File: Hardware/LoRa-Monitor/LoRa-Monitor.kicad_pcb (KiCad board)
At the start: 2 copper layers, 1.4 x 13 mm, 222 parts, among them J1 USB_C_Receptacle_USB2.0_16P, J10 AudioJack3, J11 Screw_Terminal_01x02, J12 Screw_Terminal_01x02, J13 Conn_01x02_Pin, J14 Conn_01x02_Pin, J2 Micro_SD_Card, J3 Conn_02x03_Odd_Even, J4 Conn_Coaxial, J5 Screw_Terminal_01x02, J6 Screw_Terminal_01x02, J7 AudioJack3, J8 AudioJack3, J9 Screw_Terminal_01x04, Q1 ZXTN25100DFH, Q2 ZXTN25100DFH, Q3 ZXTN25100DFH, Q4 ZXTN25100DFH, Q5 ZXTN25100DFH, Q6 ZXTN25100DFH, U1 IRM-05-5, U10 ESP32-S3-WROOM-1, U11 TPS63021DSJR, U12 NXE1S0303MC, U13 NXE1S0303MC, U14 ATM90E32AS-AU-R, U15 E22-900M30S, U16 ADuM1401xRW, U17 ADuM1401xRW, U18 ADuM1401xRW, U2 ACPL-M61L, U3 ACPL-M61L, U4 ACPL-M61L, U5 ACPL-M61L, U6 ACPL-M61L, U7 ACPL-M61L, U8 MAX3483, U9 BQ24072RGT

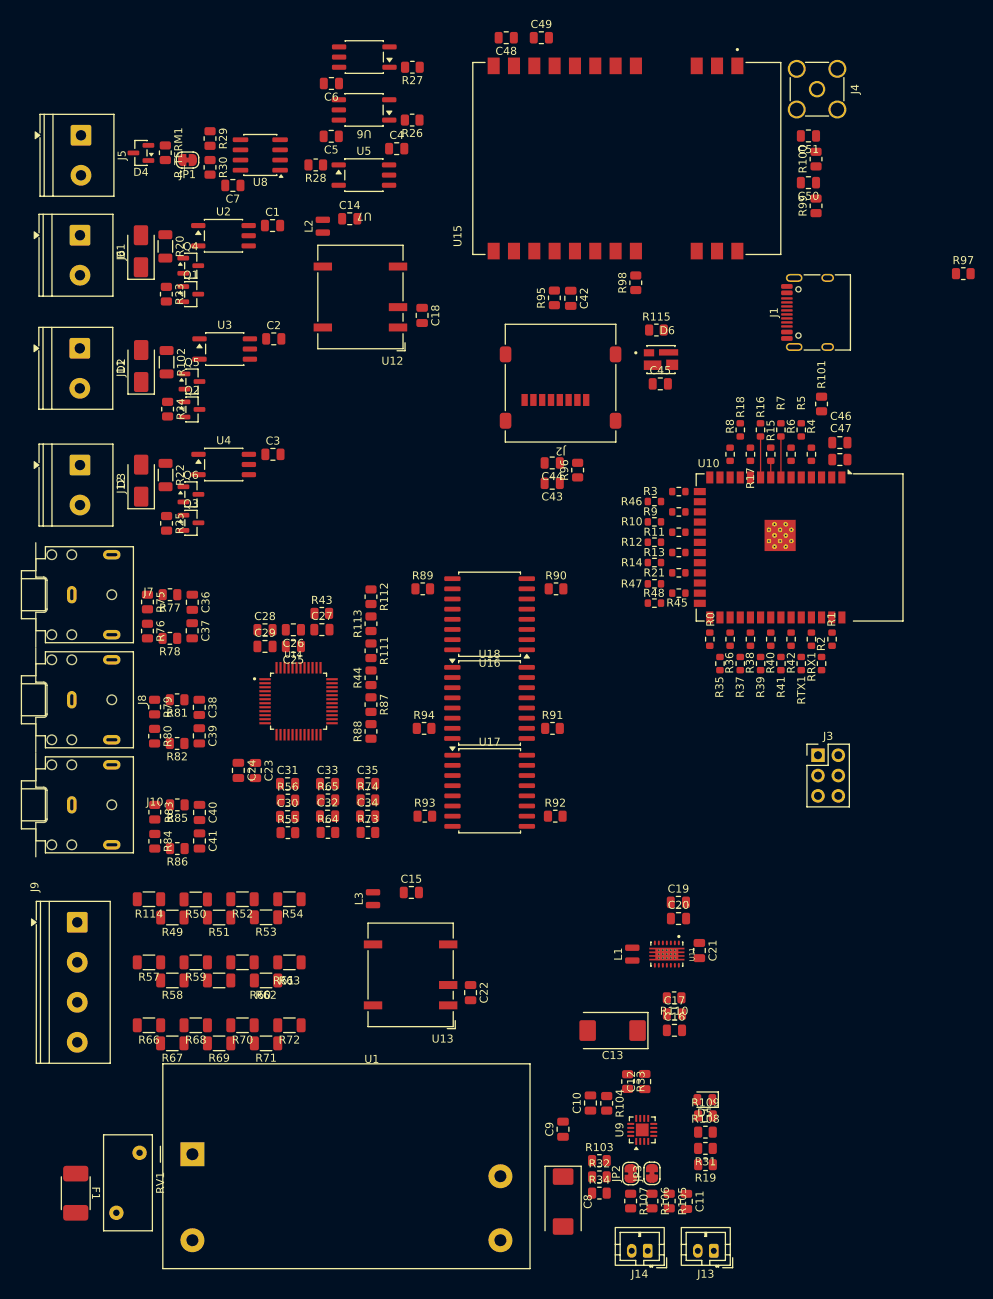
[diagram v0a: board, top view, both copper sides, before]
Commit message: Fixed schematics and started layout
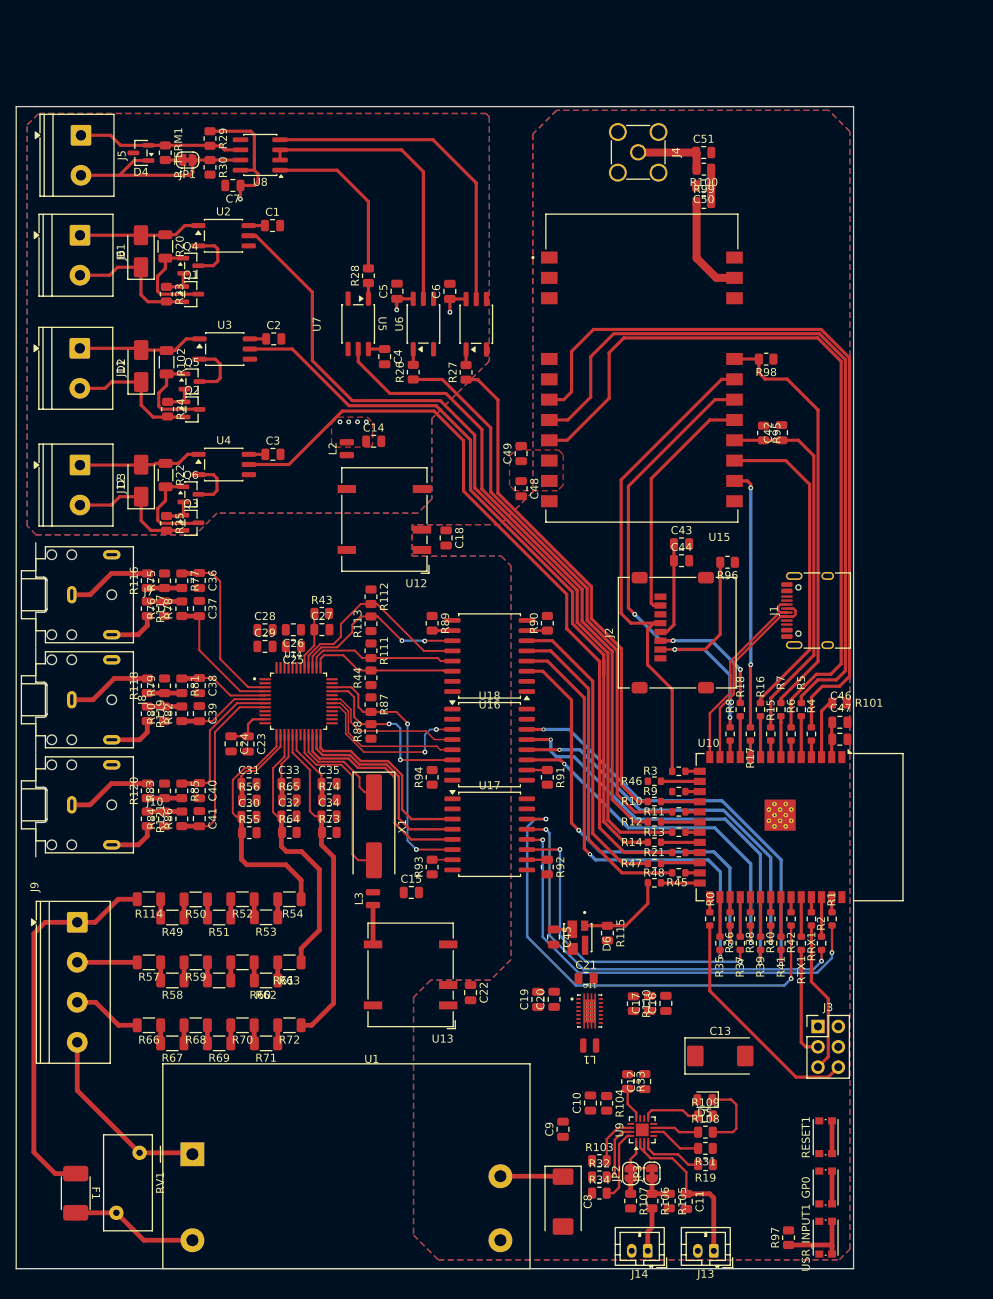
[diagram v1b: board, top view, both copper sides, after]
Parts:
- added GP0: SW_Push, Button_Switch_SMD:SW_Push_1P1T_NO_CK_KMR2, F.Cu at (130.2, 159.9)
- added R116: 0R, Resistor_SMD:R_0805_2012Metric, F.Cu at (45.4, 84.1)
- added R117: 0R, Resistor_SMD:R_0805_2012Metric, F.Cu at (45.4, 87.6)
- added R118: 0R, Resistor_SMD:R_0805_2012Metric, F.Cu at (45.4, 97.2)
- added R119: 0R, Resistor_SMD:R_0805_2012Metric, F.Cu at (45.4, 100.7)
- added R120: 0R, Resistor_SMD:R_0805_2012Metric, F.Cu at (45.4, 110.4)
- added R121: 0R, Resistor_SMD:R_0805_2012Metric, F.Cu at (45.4, 113.9)
- added RESET1: SW_Push, Button_Switch_SMD:SW_Push_1P1T_NO_CK_KMR2, F.Cu at (130.2, 153.7)
- added USR_INPUT1: SW_Push, Button_Switch_SMD:SW_Push_1P1T_NO_CK_KMR2, F.Cu at (130.2, 166.2)
- added X1: 16.384MHz, Crystal:Crystal_SMD_HC49-SD, F.Cu at (73.7, 114.8)
- moved R97 122.5 mm to (125.5, 166.2), turned to 90 degrees
- moved R115 75.6 mm to (102.9, 128.2), turned to -90 degrees
- moved D6 73.0 mm to (99.2, 128.7), turned to -90 degrees
- moved C45 70.4 mm to (96.2, 128.6), turned to -90 degrees
- moved C48 56.4 mm to (92.1, 72.6), turned to -90 degrees
- moved C49 52.0 mm to (92.1, 68.2), turned to 90 degrees
- moved R27 38.7 mm to (85.2, 58.1), turned to 90 degrees
- moved R101 37.5 mm to (131.9, 99.4), turned to 0 degrees
- moved J1 37.3 mm to (129.4, 87.8)
- moved U7 36.2 mm to (86.5, 52.0), turned to 90 degrees
- moved C46 35.0 mm to (131.9, 101.8)
- moved C47 35.0 mm to (131.9, 103.9)
- moved R0 35.0 mm to (115.7, 126.4)
- moved R1 35.0 mm to (131.0, 126.4)
- moved R10 35.0 mm to (108.8, 111.7)
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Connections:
- net Net-(R46-Pad2) renamed /MCU/USR_IN
- R18 pad 2: /MCU/CS_SD -> /MCU/SDO_SPI1
- R75 pad 1: /Connectors/IA+ -> Net-(R116-Pad1)
- R76 pad 2: /Connectors/IA- -> Net-(R117-Pad1)
- R77 pad 2: /Connectors/IA+ -> Net-(R116-Pad1)
- R78 pad 2: /Connectors/IA- -> Net-(R117-Pad1)
- R79 pad 1: /Connectors/IB+ -> Net-(R118-Pad1)
- R8 pad 1: /MCU/SDO_SPI1 -> /MCU/CS_SD
- R80 pad 2: /Connectors/IB- -> Net-(R119-Pad1)
- R81 pad 2: /Connectors/IB+ -> Net-(R118-Pad1)
- R82 pad 2: /Connectors/IB- -> Net-(R119-Pad1)
- R83 pad 1: /Connectors/IC+ -> Net-(R120-Pad1)
- R84 pad 2: /Connectors/IC- -> Net-(R121-Pad1)
- R85 pad 2: /Connectors/IC+ -> Net-(R120-Pad1)
- R86 pad 2: /Connectors/IC- -> Net-(R121-Pad1)
- U17 pad 11: /Energy meter/ZX0 -> /Energy meter/PM1
- U17 pad 12: /Energy meter/ZX1 -> /Energy meter/ZX0
- U17 pad 13: /Energy meter/ZX2 -> /Energy meter/ZX1
- U17 pad 14: /Energy meter/WARNOUT -> /Energy meter/ZX2
- U17 pad 3: /Energy meter/WARNOUT_M90 -> /Energy meter/ZX2_M90
- U17 pad 4: /Energy meter/ZX2_M90 -> /Energy meter/ZX1_M90
- U17 pad 5: /Energy meter/ZX1_M90 -> /Energy meter/ZX0_M90
- U17 pad 6: /Energy meter/ZX0_M90 -> /Energy meter/PM1_M90
- U18 pad 11: /Energy meter/IRQ0 -> /Energy meter/PM0
- U18 pad 12: /Energy meter/IRQ1 -> /Energy meter/IRQ0
- U18 pad 13: /Energy meter/PM0 -> /Energy meter/IRQ1
- U18 pad 14: /Energy meter/PM1 -> /Energy meter/WARNOUT
- U18 pad 3: /Energy meter/PM1_M90 -> /Energy meter/WARNOUT_M90
- U18 pad 4: /Energy meter/PM0_M90 -> /Energy meter/IRQ1_M90
- U18 pad 5: /Energy meter/IRQ1_M90 -> /Energy meter/IRQ0_M90
- U18 pad 6: /Energy meter/IRQ0_M90 -> /Energy meter/PM0_M90
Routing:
- net /Energy Meter Interface Module/PULSE_IN1_3V3: track 0.00 -> 107.3 mm
- net /Energy Meter Interface Module/PULSE_IN3_3V3: track 0.00 -> 96.9 mm
- net /LoRa Module/DIO2_E22: track 0.00 -> 95.7 mm
- net /Energy Meter Interface Module/PULSE_IN2_3V3: track 0.00 -> 95.4 mm
- net /LoRa Module/RXEN_E22: track 0.00 -> 95.0 mm
- net /LoRa Module/TXEN_E22: track 0.00 -> 92.3 mm
- net /Energy Meter Interface Module/RXD_485: track 0.00 -> 79.2 mm
- net /Energy Meter Interface Module/EN_485: track 0.00 -> 72.3 mm
- net /Energy Meter Interface Module/TXD_485: track 0.00 -> 63.7 mm
- net /MCU/SCLK_SPI1: track 0.00 -> 62.4 mm
- net /Energy meter/ZX2: track 0.00 -> 61.4 mm, vias 0 -> 2
- net /Energy meter/SCKL_SPI0: track 0.00 -> 57.6 mm, vias 0 -> 2
- net /Energy meter/ZX0: track 0.00 -> 57.0 mm, vias 0 -> 2
- net /Energy meter/CS_ATM90: track 0.00 -> 56.6 mm, vias 0 -> 2
- net /MCU/SDO_SPI1: track 0.00 -> 55.9 mm, vias 0 -> 3
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- added copper zone on F.Cu, net +3.3V
- added copper zone on F.Cu, net +3.3V_485
- added copper zone on In2.Cu, net +3.3V_485
- added copper zone on B.Cu, net GND
- added copper zone on F.Cu, net GND
- added copper zone on In1.Cu, net GND
- added copper zone on B.Cu, net GND_485
- added copper zone on F.Cu, net GND_485
- added copper zone on In1.Cu, net GND_485
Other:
- board size 1.4 x 13 mm -> 104.7 x 145.3 mm
- copper layers 2 -> 4

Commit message: Finished routing and DRC gives 0 errors.
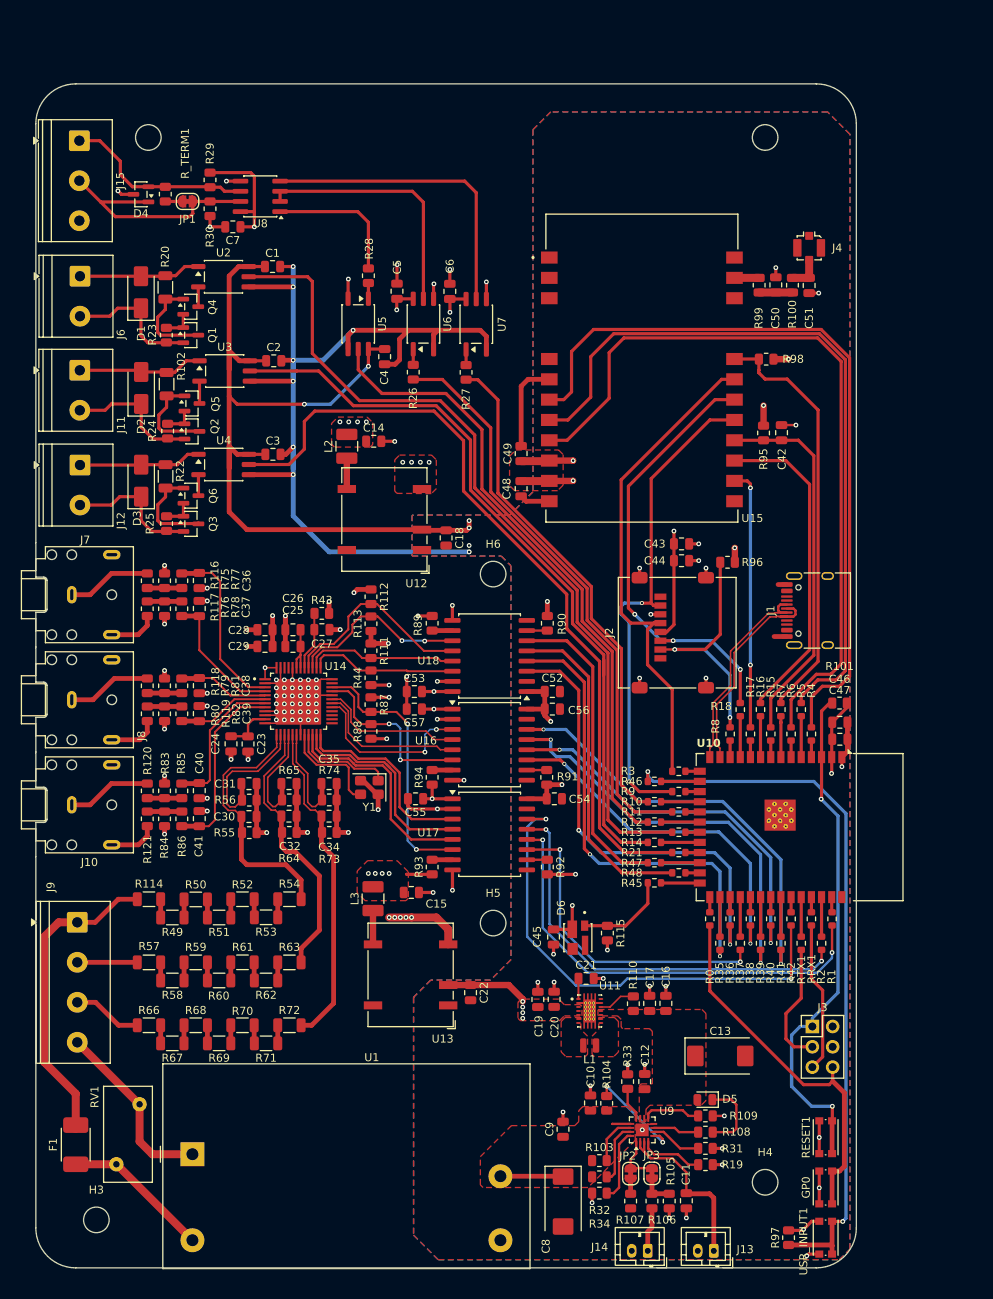
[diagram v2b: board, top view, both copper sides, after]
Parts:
- removed J5: Screw_Terminal_01x02, TerminalBlock_Phoenix:TerminalBlock_Phoenix_PT-1,5-2-5.0-H_1x02_P5.00mm_Horizontal
- removed X1: 16.384MHz, Crystal:Crystal_SMD_HC49-SD
- added C52: 100nF, Capacitor_SMD:C_0805_2012Metric, F.Cu at (96.0, 98.0)
- added C53: 100nF, Capacitor_SMD:C_0805_2012Metric, F.Cu at (78.8, 98.0)
- added C54: 100nF, Capacitor_SMD:C_0805_2012Metric, F.Cu at (96.2, 111.4)
- added C55: 100nF, Capacitor_SMD:C_0805_2012Metric, F.Cu at (78.9, 111.4)
- added C56: 100nF, Capacitor_SMD:C_0805_2012Metric, F.Cu at (96.0, 100.2)
- added C57: 100nF, Capacitor_SMD:C_0805_2012Metric, F.Cu at (78.8, 100.2)
- added H1: MountingHole, MountingHole:MountingHole_3.2mm_M3_DIN965, F.Cu at (122.6, 28.7)
- added H2: MountingHole, MountingHole:MountingHole_3.2mm_M3_DIN965, F.Cu at (45.5, 28.7)
- added H3: MountingHole, MountingHole:MountingHole_3.2mm_M3_DIN965, F.Cu at (39.0, 164.0)
- added H4: MountingHole, MountingHole:MountingHole_3.2mm_M3_DIN965, F.Cu at (122.6, 159.3)
- added H5: MountingHole, MountingHole:MountingHole_3.2mm_M3_DIN965, F.Cu at (88.6, 126.9)
- added H6: MountingHole, MountingHole:MountingHole_3.2mm_M3_DIN965, F.Cu at (88.6, 83.3)
- added J15: Screw_Terminal_01x03, TerminalBlock_Phoenix:TerminalBlock_Phoenix_PT-1,5-3-5.0-H_1x03_P5.00mm_Horizontal, F.Cu at (36.9, 29.1)
- added Y1: 16.384MHz, Crystal:Crystal_SMD_3225-4Pin_3.2x2.5mm, F.Cu at (73.1, 110.0)
- J4: footprint Connector_Coaxial:SMA_Amphenol_901-144_Vertical -> Connector_Coaxial:U.FL_Molex_MCRF_73412-0110_Vertical
- L2, L3: footprint DeviceComponents:L_0806_2016Metric -> Inductor_SMD:L_1210_3225Metric_Pad1.42x2.65mm_HandSolder
- moved J4 24.5 mm to (128.1, 42.5), turned to 0 degrees
- moved C51 21.2 mm to (128.1, 47.2), turned to -90 degrees
- moved R100 18.2 mm to (126.0, 47.2), turned to 90 degrees
- moved C50 15.3 mm to (123.9, 47.1), turned to 90 degrees
- moved R99 12.4 mm to (121.8, 47.2), turned to -90 degrees
- moved F1 6.07 mm to (36.4, 154.4)
- moved RV1 6.07 mm to (41.5, 157.1)
- moved C7 5.18 mm to (56.1, 39.9)
- moved R_TERM1 5.18 mm to (47.6, 35.8)
- moved D4 5.18 mm to (44.6, 35.8)
- moved U8 5.18 mm to (59.5, 36.1)
- moved JP1 5.17 mm to (50.4, 36.7)
- moved R29 5.17 mm to (53.2, 34.0)
- moved R30 5.17 mm to (53.2, 37.6)
- moved C1 5.12 mm to (61.0, 44.8)
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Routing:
- net GND: track 0.00 -> 194.2 mm, vias 0 -> 41
- net GND_M90: track 23.7 -> 187.8 mm, vias 0 -> 70
- net +3.3V: track 27.2 -> 185.5 mm, vias 0 -> 21
- net /MCU/USR_IN: track 9.57 -> 90.6 mm, vias 0 -> 2
- net /Connectors/ESP_EN: track 11.6 -> 71.3 mm, vias 0 -> 2
- net +3.3V_M90: track 0.00 -> 37.6 mm, vias 0 -> 17
- net /MCU/SDI_SPI1: track 30.3 -> 62.4 mm, vias 0 -> 2
- net GND_485: track 0.00 -> 19.5 mm, vias 0 -> 13
- net /Connectors/GPIO0: track 33.3 -> 47.5 mm
- net Net-(U9-EN2): track 0.00 -> 12.8 mm, vias 0 -> 2
- net /LoRa Module/ANT: track 12.7 -> 3.08 mm
- net Net-(U14-OSCI): track 22.2 -> 13.1 mm
- net /Connectors/Ua: track 48.4 -> 39.2 mm
- net /Energy meter/VAN: track 11.0 -> 17.8 mm
- net VDD18: track 0.00 -> 6.61 mm
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- added copper zone on In2.Cu, net +3.3V
- added copper zone on F.Cu, net +3.3V_M90
- added copper zone on In2.Cu, net +3.3V_M90
- added copper zone on F.Cu, net +5V
- added copper zone on In1.Cu, net GND_M90
- added copper zone on F.Cu, net Net-(U11-L1_8)
- added copper zone on F.Cu, net Net-(U11-L2_6)
- added copper zone on F.Cu, net VBUS
- removed copper zone on B.Cu, net GND_485
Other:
- board size 104.7 x 145.3 mm -> 102.6 x 148 mm

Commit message: Added parameters for the productions files, changed components on LCSC to reduce the price of BoM, minimal changes on the routing.
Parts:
- added C58: 100nF, Capacitor_SMD:C_0805_2012Metric, F.Cu at (123.2, 166.2)
- added G***: LOGO, LOGO, F.Cu at (74.5, 35.6)
- C1, C2, C3, C4, C5, C6, C7: value 0.1 uF -> 100nF 50V X7R
- C12: value 4.7uF 50V X7R -> 4.7uF 25V X7R
- C17, C21, C24, C26, C27, C28, C29, C42, C43, C45, C47, C49, C52, C53, C54, C55, C56, C57: value 100nF -> 100nF 50V X7R
- C18, C22: value 1uF -> 1uF 50V X7R
- C31, C33, C35: value 18nf -> 18nF
- Q1, Q2, Q3, Q4, Q5, Q6: value ZXTN25100DFH -> MMBT5551L
- U8: value MAX3483 -> MAX3485
- moved F1 1.01 mm to (35.5, 154.0)
- moved U1 0.73 mm to (50.3, 155.5)
- moved RV1 0.68 mm to (41.0, 156.7)
- moved C8 0.34 mm to (97.3, 161.4)
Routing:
- net /Energy Meter Interface Module/PULSE_IN2_3V3: track 94.5 -> 90.1 mm
- net GND_M90: track 187.8 -> 184.5 mm
- net /Energy Meter Interface Module/PULSE_IN1_3V3: track 105.4 -> 102.5 mm
- net /Energy Meter Interface Module/RXD_485: track 79.7 -> 77.2 mm
- net /MCU/USR_IN: track 90.6 -> 92.9 mm
- net /Energy meter/SDI: track 25.5 -> 27.8 mm
- net /Energy Meter Interface Module/PULSE_IN3_3V3: track 98.9 -> 96.8 mm
- net /LoRa Module/DIO2_E22: track 95.7 -> 97.7 mm
- net /Energy Meter Interface Module/EN_485: track 72.3 -> 70.7 mm
- net /LoRa Module/TXEN_E22: track 92.3 -> 93.7 mm
- net /Energy meter/CS_ATM90: track 57.8 -> 58.9 mm
- net /Energy meter/SCKL_SPI0: track 58.6 -> 59.5 mm
- net /Connectors/Ua: track 39.2 -> 38.3 mm
- net Net-(U1-AC/L): track 18.5 -> 19.4 mm
- net GND: track 194.2 -> 195.0 mm
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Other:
- board text added: "Boot Design 2026 FIUBA ARG"
